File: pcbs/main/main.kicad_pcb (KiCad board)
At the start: 2 copper layers, 114 x 123.3 mm, 67 parts, among them J1 JST_XH_B3B, J2 JST_XH_B3B, J3 XT30PW-M, Q1 2SC945, Q2 2SC945, Q3 2SC945, Q4 2SC945, Q5 2SC945, Q6 2SC945, Q7 2SC945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

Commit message: Start layout
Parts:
- moved as3 189.5 mm to (79.1, 43.5)
- moved as4 189.5 mm to (79.1, 50.8)
- moved as1 162.9 mm to (101.0, 66.7), turned to 180 degrees
- moved C13 145.5 mm to (83.8, 124.7), turned to -90 degrees
- moved JP2 133.6 mm to (102.7, 71.6)
- moved JP1 132.6 mm to (99.2, 71.6)
- moved C5 129.1 mm to (97.0, 113.0), turned to -90 degrees
- moved C6 125.1 mm to (100.0, 113.0), turned to -90 degrees
- moved C7 121.3 mm to (103.0, 113.0), turned to -90 degrees
- moved C10 120.7 mm to (108.3, 51.8), turned to -173 degrees
- moved C12 119.8 mm to (108.3, 138.1), turned to 83 degrees
- moved C8 117.5 mm to (106.0, 113.0), turned to -90 degrees
- moved C2 106.9 mm to (139.2, 138.4), turned to 27.2 degrees
- moved C9 105.4 mm to (115.3, 138.1), turned to 83 degrees
- moved C3 103.7 mm to (113.9, 52.2), turned to 7 degrees
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
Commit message: Fix jumpers
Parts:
- removed JP1, JP2, JP3, JP4, JP5, JP6, JP7, JP8: Jumper_2_Open, Connector_PinHeader_2.54mm:PinHeader_1x02_P2.54mm_Vertical
- added J2: Jumpers, Connector_PinHeader_2.54mm:PinHeader_2x08_P2.54mm_Vertical, F.Cu at (106.1, 69.8)
- moved as2 151.5 mm to (100.4, 64.0), turned to 90 degrees
- moved as3 25.5 mm to (94.2, 64.0), turned to 90 degrees
- moved as4 15.8 mm to (87.8, 64.0), turned to 90 degrees
- moved as1 6.28 mm to (106.7, 64.0), turned to 90 degrees
- renumbered J2 to J3, J3 to J4
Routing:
- net /esp32/I2C.SDA: track 5.82 -> 34.5 mm
- net /esp32/I2C.SCL: track 6.50 -> 34.3 mm
- net Net-(J2-Pin_1): track 0.00 -> 8.69 mm
- net Net-(J2-Pin_9): track 0.00 -> 8.25 mm
- net Net-(J2-Pin_5): track 0.00 -> 8.21 mm
- net Net-(J2-Pin_13): track 0.00 -> 8.08 mm
- net Net-(J2-Pin_3): track 0.00 -> 6.01 mm
- net Net-(J2-Pin_7): track 0.00 -> 5.53 mm
- net Net-(J2-Pin_11): track 0.00 -> 5.04 mm
- net Net-(J2-Pin_15): track 0.00 -> 4.52 mm

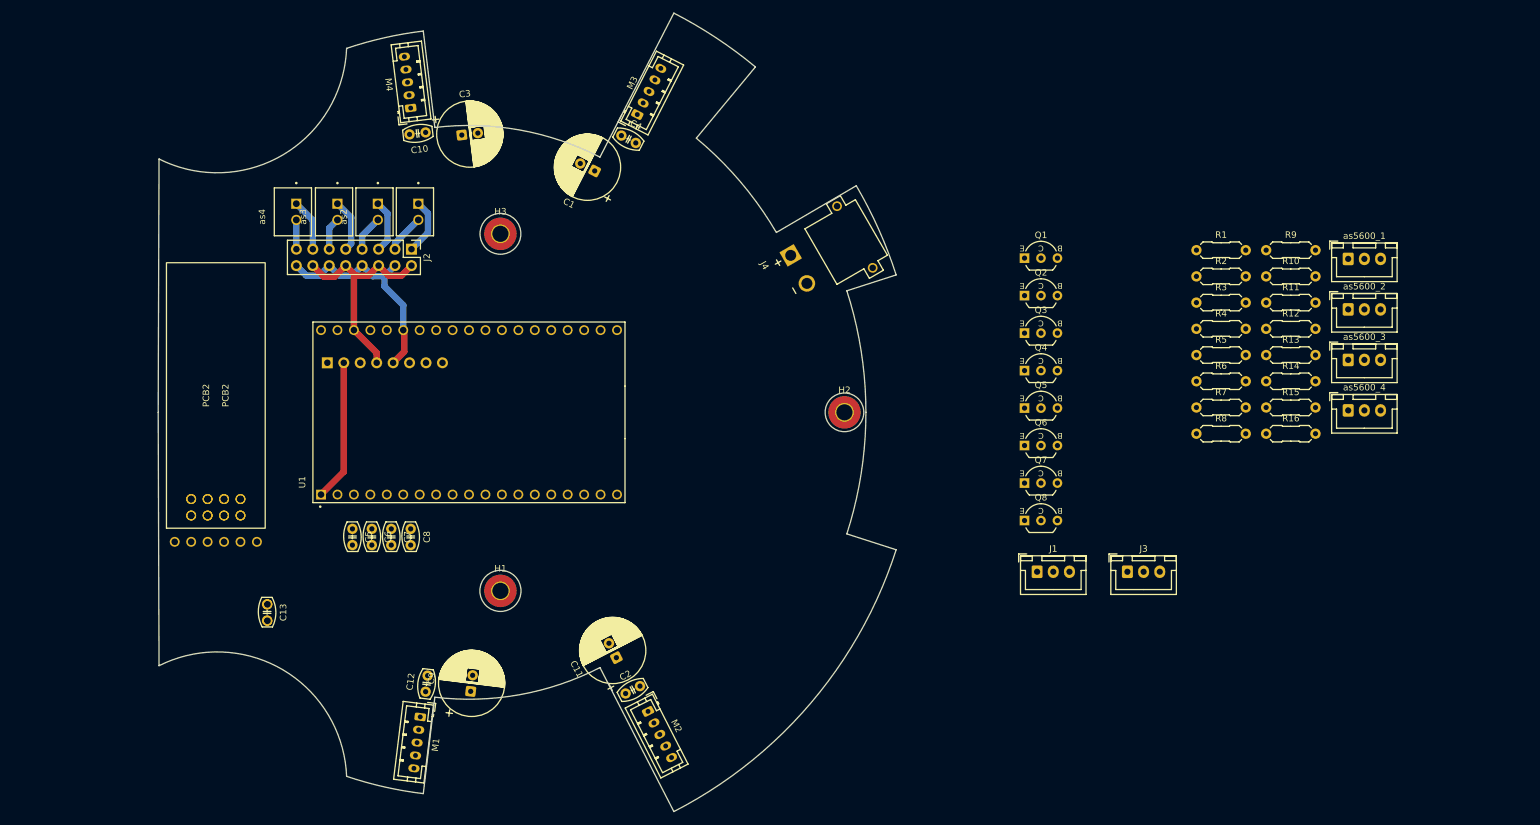
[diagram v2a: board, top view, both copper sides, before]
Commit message: Preliminary placing components
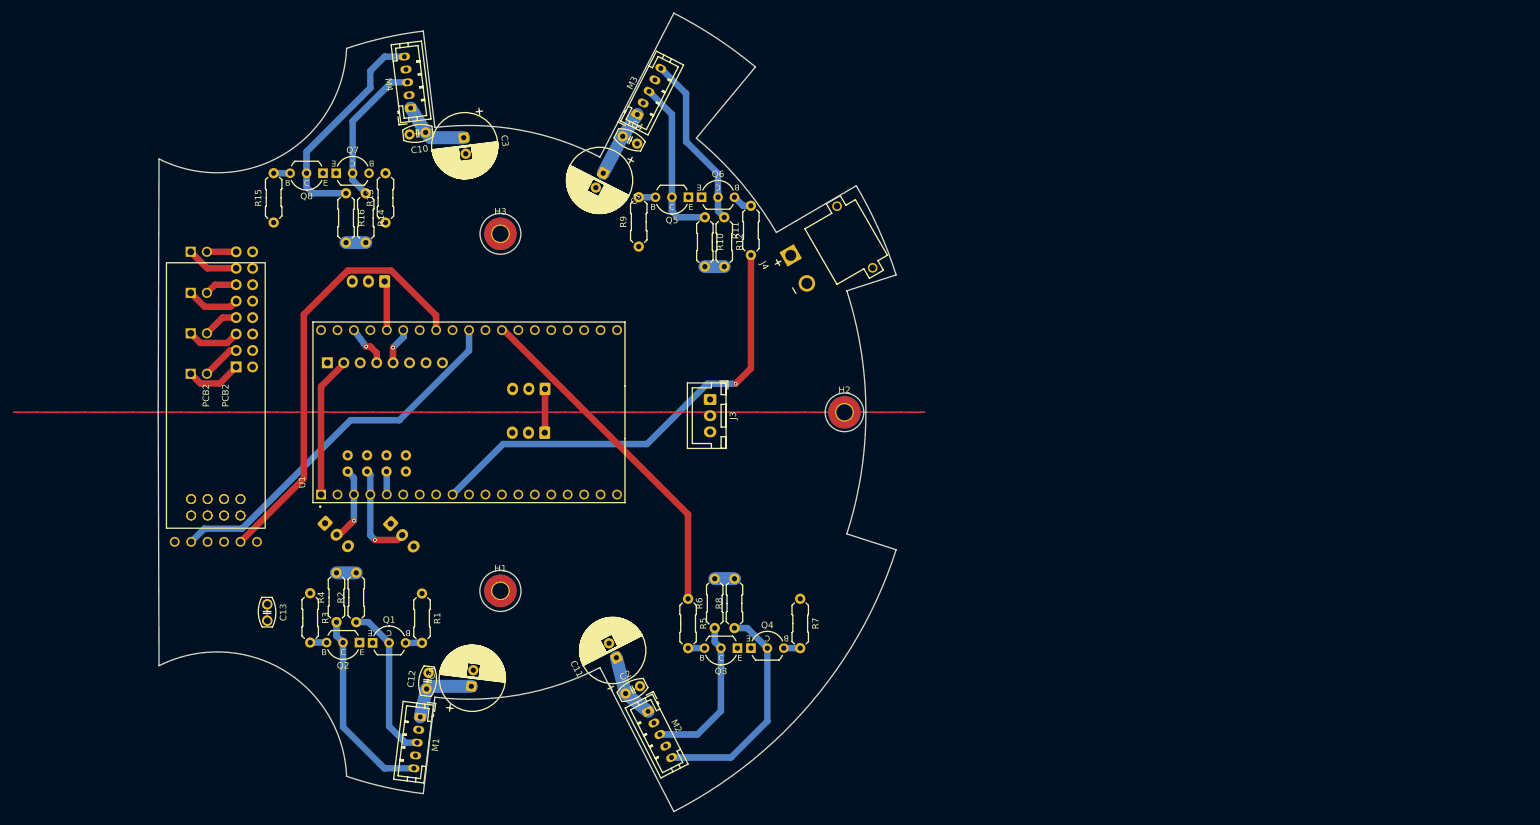
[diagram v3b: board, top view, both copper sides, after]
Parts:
- C5, C6, C7, C8, J1, J2, as1, as2, as3, as4, as5600_1, as5600_2, as5600_3, as5600_4: moved to B.Cu
- moved as5600_1 163.2 mm to (92.8, 112.1), turned to -45 degrees
- moved R15 155.9 mm to (84.8, 65.7), turned to 90 degrees
- moved as5600_2 151.5 mm to (102.9, 112.2), turned to -45 degrees
- moved R16 146.9 mm to (96.0, 61.2), turned to -90 degrees
- moved R3 144.1 mm to (90.5, 122.9), turned to -90 degrees
- moved R14 142.1 mm to (99.1, 61.2), turned to -90 degrees
- moved R4 140.3 mm to (94.5, 127.4), turned to 90 degrees
- moved R2 140.3 mm to (97.6, 127.4), turned to 90 degrees
- moved R13 137.6 mm to (102.1, 65.7), turned to 90 degrees
- moved R1 130.8 mm to (107.7, 123.0), turned to -90 degrees
- moved as5600_4 124.2 mm to (126.7, 98.1), turned to 180 degrees
- moved as5600_3 124.1 mm to (126.7, 91.4), turned to 180 degrees
- moved Q8 120.9 mm to (92.5, 58.1), turned to 180 degrees
- moved Q1 116.9 mm to (100.1, 130.6)
- moved Q7 116.6 mm to (94.5, 58.1)
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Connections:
- J3 pad 3: +3.3V -> +5V
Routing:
- net /esp32/M3_PWM: track 0.00 -> 71.7 mm, vias 0 -> 1
- net /esp32/RADIO.MISO: track 0.00 -> 67.5 mm
- net /esp32/RADIO.CS: track 0.00 -> 58.3 mm
- net /esp32/M2_DIR: track 0.00 -> 53.6 mm
- net +24V: track 0.00 -> 46.7 mm
- net Net-(M2-PWM): track 0.00 -> 34.8 mm
- net Net-(M4-PWM): track 0.00 -> 34.7 mm
- net Net-(M1-PWM): track 0.00 -> 30.2 mm
- net /esp32/I2C.SDA: track 34.5 -> 5.74 mm, vias 0 -> 1
- net Net-(M3-PWM): track 0.00 -> 27.8 mm
- net Net-(M3-DIR): track 0.00 -> 27.6 mm
- net /esp32/I2C.SCL: track 34.3 -> 6.73 mm, vias 0 -> 1
- net Net-(M1-DIR): track 0.00 -> 24.7 mm
- net Net-(M2-DIR): track 0.00 -> 24.2 mm
- net Net-(M4-DIR): track 0.00 -> 22.9 mm
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- added copper zone on B.Cu, net GND
- added copper zone on F.Cu, net GND

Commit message: Add step file
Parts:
- turned C12 to 173 degrees
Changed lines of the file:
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@@
 	(footprint "PCM_Capacitor_THT_AKL:C_Disc_D5.0mm_W2.5mm_P2.50mm"
 		(layer "F.Cu")
-		(at 108.458 137.7188 83)
+		(at 108.458 137.7188 173)
 		(descr "C, Disc series, Radial, pin pitch=2.50mm, , diameter*width=5*2.5mm^2, Capacitor, http://cdn-reichelt.de/documents/datenblatt/B300/DS_KERKO_TC.pdf, Alternate KiCad Library")
 		(tags "C Disc series Radial pin pitch 2.50mm  diameter 5mm width 2.5mm Capacitor")
 		(property "Reference" "C12"
-			(at 1.25 -2.5 83)
+			(at 1.25 -2.5 173)
 			(layer "F.SilkS")
 			(effects
@@
 		)
 		(property "Value" "100 nF"
-			(at 1.25 2.5 83)
+			(at 1.25 2.5 173)
 			(layer "F.Fab")
 			(hide yes)
@@
 		)
 		(property "Datasheet" "~"
-			(at 0 0 83)
+			(at 0 0 173)
 			(layer "F.Fab")
 			(hide yes)
@@
 		)
 		(property "Description" "Unpolarized capacitor"
-			(at 0 0 83)
+			(at 0 0 173)
 			(layer "F.Fab")
 			(hide yes)
@@
 		)
 		(fp_line
+			(start 1.524 0)
+			(end 1.397 0)
+			(stroke
+				(width 0.12)
+				(type solid)
+			)
+			(layer "F.SilkS")
+		)
+		(fp_line
+			(start 1.397 0)
+			(end 1.397 -0.6)
+			(stroke
+				(width 0.12)
+				(type solid)
+			)
+			(layer "F.SilkS")
+		)
+		(fp_line
+			(start 1.397 0)
+			(end 1.397 0.6)
+			(stroke
+				(width 0.12)
+				(type solid)
+			)
+			(layer "F.SilkS")
+		)
+		(fp_line
+			(start 1.1 0)
+			(end 1.1 -0.6)
+			(stroke
+				(width 0.12)
+				(type solid)
+			)
+			(layer "F.SilkS")
+		)
+		(fp_line
+			(start 1.1 0)
+			(end 1.1 0.6)
+			(stroke
+				(width 0.12)
+				(type solid)
+			)
+			(layer "F.SilkS")
+		)
+		(fp_line
 			(start 0.973 0)
 			(end 1.1 0)
@@
 		)
 		(fp_line
-			(start 1.1 0)
-			(end 1.1 -0.6)
-			(stroke
-				(width 0.12)
-				(type solid)
-			)
-			(layer "F.SilkS")
-		)
-		(fp_line
-			(start 1.1 0)
-			(end 1.1 0.6)
-			(stroke
-				(width 0.12)
-				(type solid)
-			)
-			(layer "F.SilkS")
-		)
-		(fp_line
-			(start 1.397 0)
-			(end 1.397 -0.6)
-			(stroke
-				(width 0.12)
-				(type solid)
-			)
-			(layer "F.SilkS")
-		)
-		(fp_line
-			(start 1.397 0)
-			(end 1.397 0.6)
-			(stroke
-				(width 0.12)
-				(type solid)
-			)
-			(layer "F.SilkS")
-		)
-		(fp_line
-			(start 1.524 0)
-			(end 1.397 0)
-			(stroke
-				(width 0.12)
-				(type solid)
-			)
-			(layer "F.SilkS")
-		)
-		(fp_line
 			(start -1.0795 0.8255)
 			(end -1.0795 -0.762)
+			(stroke
+				(width 0.12)
+				(type solid)
+			)
+			(layer "F.SilkS")
+		)
+		(fp_arc
+			(start 3.491127 0.759477)
+			(mid 1.21396 1.356434)
+			(end -1.0795 0.8255)
 			(stroke
 				(width 0.12)
@@
 			(layer "F.SilkS")
 		)
-		(fp_arc
-			(start 3.491127 0.759477)
-			(mid 1.21396 1.356434)
-			(end -1.0795 0.8255)
-			(stroke
-				(width 0.12)
-				(type solid)
-			)
-			(layer "F.SilkS")
+		(fp_line
+			(start 4 -1.5)
+			(end -1.5 -1.5)
+			(stroke
+				(width 0.05)
+				(type solid)
+			)
+			(layer "F.CrtYd")
+		)
+		(fp_line
+			(start 4 1.5)
+			(end 4 -1.5)
+			(stroke
+				(width 0.05)
+				(type solid)
+			)
+			(layer "F.CrtYd")
 		)
 		(fp_line
@@
 		)
 		(fp_line
-			(start 4 -1.5)
-			(end -1.5 -1.5)
-			(stroke
-				(width 0.05)
-				(type solid)
-			)
-			(layer "F.CrtYd")
-		)
-		(fp_line
 			(start -1.5 1.5)
 			(end 4 1.5)
@@
 		)
 		(fp_line
-			(start 4 1.5)
-			(end 4 -1.5)
-			(stroke
-				(width 0.05)
-				(type solid)
-			)
-			(layer "F.CrtYd")
+			(start 3.75 -1.25)
+			(end -1.25 -1.25)
+			(stroke
+				(width 0.1)
+				(type solid)
+			)
+			(layer "F.Fab")
+		)
+		(fp_line
+			(start 3.75 1.25)
+			(end 3.75 -1.25)
+			(stroke
+				(width 0.1)
+				(type solid)
+			)
+			(layer "F.Fab")
 		)
 		(fp_line
@@
 		)
 		(fp_line
-			(start 3.75 -1.25)
-			(end -1.25 -1.25)
-			(stroke
-				(width 0.1)
-				(type solid)
-			)
-			(layer "F.Fab")
-		)
-		(fp_line
 			(start -1.25 1.25)
 			(end 3.75 1.25)
@@
 			(layer "F.Fab")
 		)
-		(fp_line
-			(start 3.75 1.25)
-			(end 3.75 -1.25)
-			(stroke
-				(width 0.1)
-				(type solid)
-			)
-			(layer "F.Fab")
-		)
 		(fp_text user "${REFERENCE}"
-			(at 1.25 0 83)
+			(at 1.25 0 173)
 			(layer "F.Fab")
 			(effects
@@
 		)
 		(pad "1" thru_hole circle
-			(at 0 0 83)
+			(at 0 0 173)
 			(size 1.6 1.6)
 			(drill 0.8)
@@
 		)
 		(pad "2" thru_hole circle
-			(at 2.5 0 83)
+			(at 2.5 0 173)
 			(size 1.6 1.6)
 			(drill 0.8)

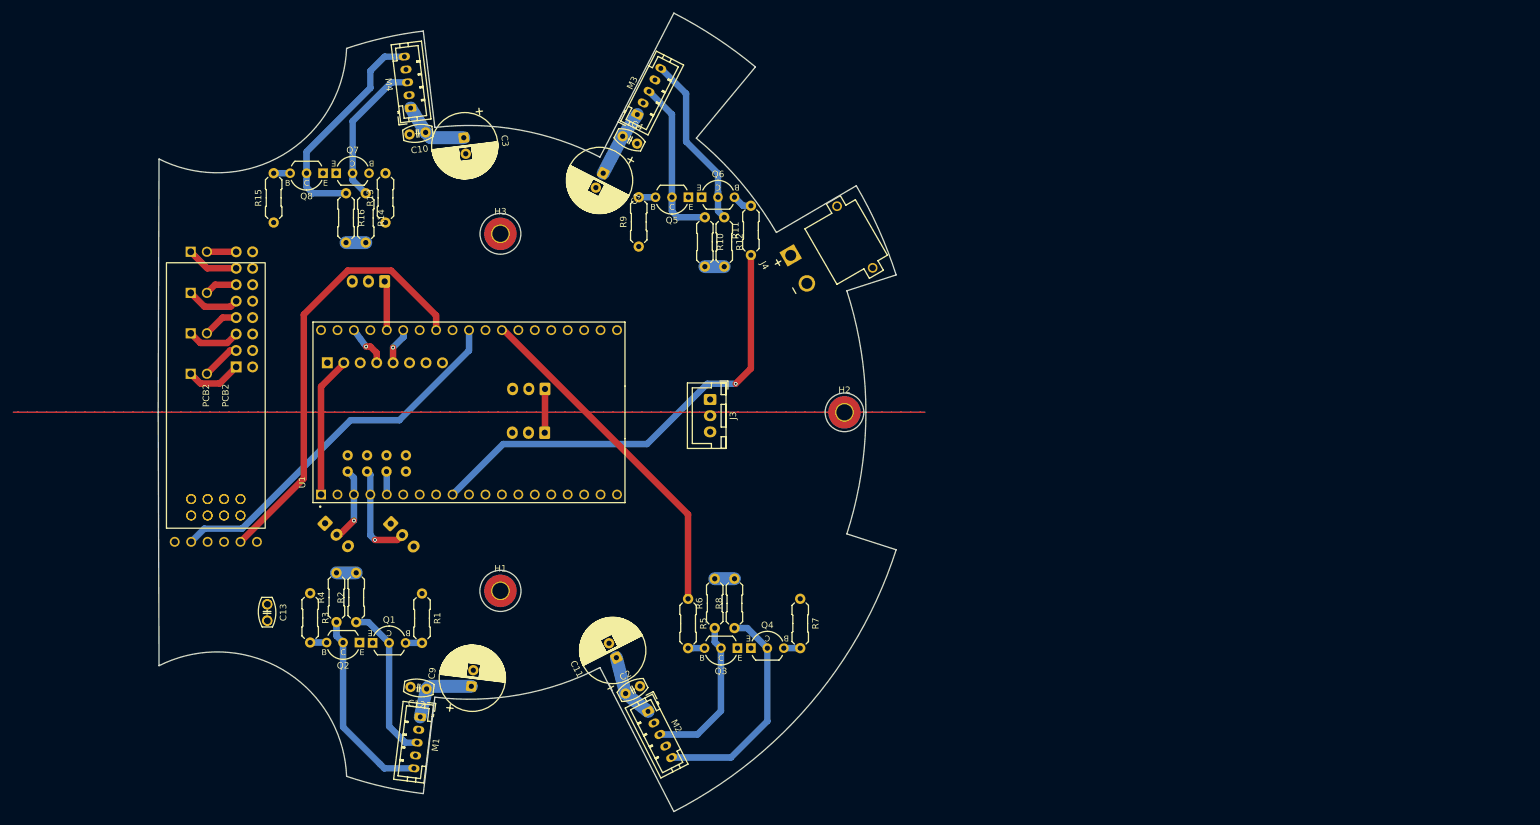
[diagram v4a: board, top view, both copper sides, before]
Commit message: feat: roteamento do main PCB
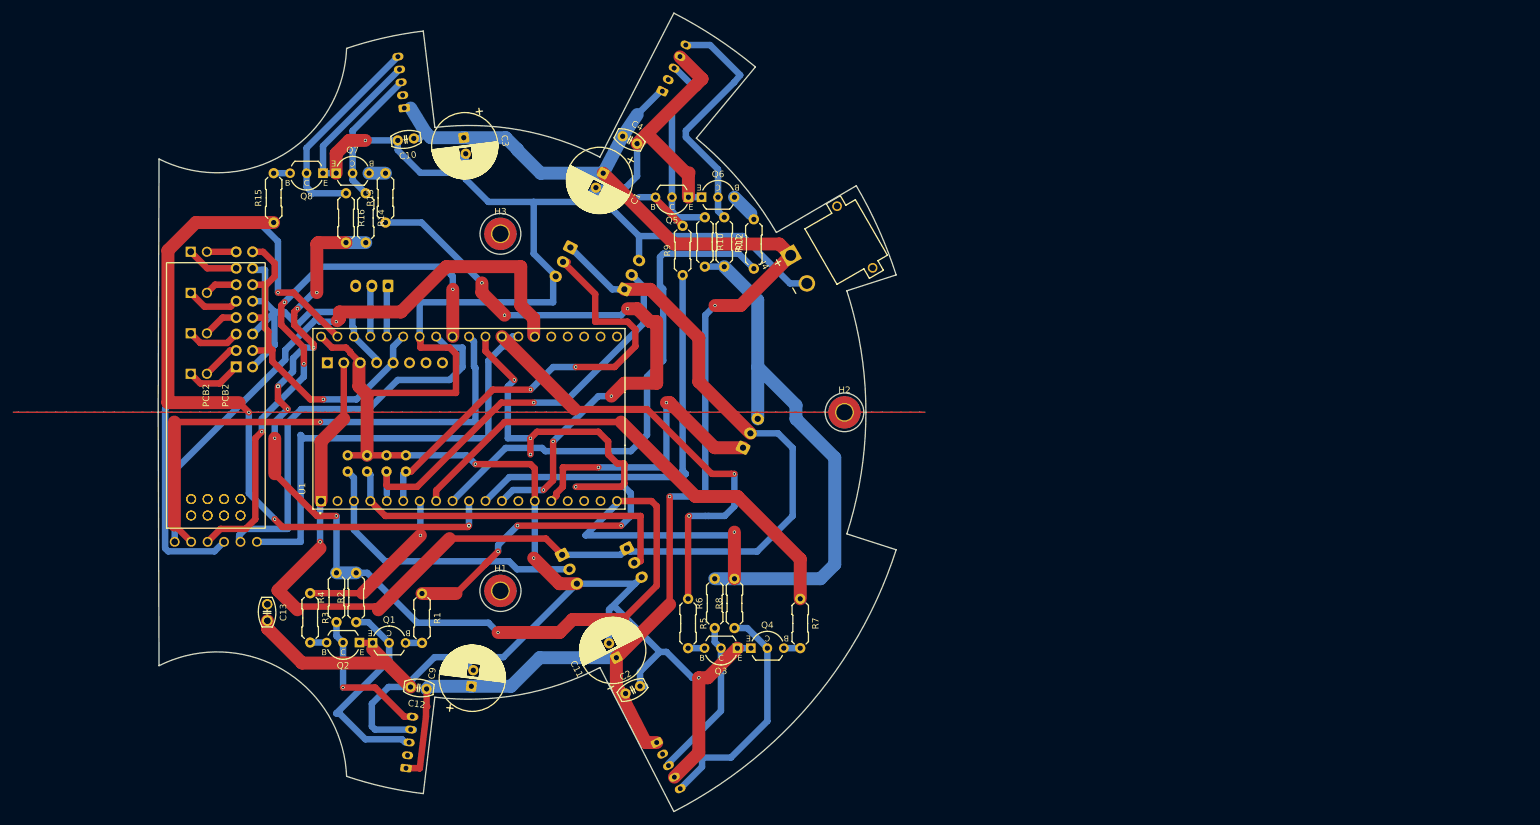
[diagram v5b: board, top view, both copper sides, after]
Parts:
- J3, M1, M2, M3, M4: moved to B.Cu
- moved as5600_1 36.9 mm to (129.4, 117.0), turned to -63 degrees
- moved as5600_2 36.7 mm to (139.4, 116.0), turned to -63 degrees
- moved as5600_4 28.9 mm to (130.7, 69.5), turned to -117 degrees
- moved as5600_3 19.7 mm to (139.0, 76.0), turned to 63 degrees
- moved J3 9.02 mm to (157.3, 100.5), turned to 63 degrees
- moved M1 8.21 mm to (105.3, 150.0), turned to 83 degrees
- moved R9 8.09 mm to (148.0, 73.8)
- moved M3 5.29 mm to (144.9, 45.4)
- moved M2 4.99 mm to (144.0, 146.0)
- moved R11 2.14 mm to (159.0, 72.8)
- moved C10 2.05 mm to (106.5, 52.7)
- moved M4 1.00 mm to (105.0, 48.0)
- moved U1 1.00 mm to (115.0, 96.0)
- moved J1 0.87 mm to (102.5, 75.5)
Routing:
- net GND: track 0.00 -> 474.5 mm, vias 0 -> 4
- net +5V: track 12.1 -> 268.0 mm, vias 0 -> 9
- net +24V: track 46.7 -> 228.4 mm, vias 0 -> 2
- net +3.3V: track 28.6 -> 190.6 mm, vias 0 -> 1
- net /esp32/M4_PWM: track 0.00 -> 107.3 mm, vias 0 -> 3
- net /esp32/M1_DIR: track 0.00 -> 104.5 mm, vias 0 -> 7
- net /esp32/RADIO.MOSI: track 0.00 -> 95.7 mm, vias 0 -> 1
- net /esp32/M4_DIR: track 0.00 -> 94.4 mm, vias 0 -> 6
- net /esp32/RADIO.CE: track 0.00 -> 90.7 mm, vias 0 -> 1
- net /esp32/RADIO.CLK: track 0.00 -> 85.3 mm, vias 0 -> 4
- net /esp32/M2_PWM: track 0.00 -> 77.1 mm
- net /esp32/RADIO.IRQ: track 0.00 -> 70.9 mm
- net /esp32/M4_ENC: track 0.00 -> 69.5 mm, vias 0 -> 2
- net /esp32/M3_DIR: track 0.00 -> 63.6 mm
- net /esp32/M3_ENC: track 3.61 -> 64.2 mm, vias 0 -> 1
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
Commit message: Re-routing
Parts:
- J3: moved to F.Cu
- moved as5600_2 57.4 mm to (88.6, 89.2), turned to 0 degrees
- moved C13 54.6 mm to (72.0, 71.3), turned to 90 degrees
- moved J3 46.4 mm to (113.2, 114.8), turned to 180 degrees
- moved as5600_1 43.9 mm to (88.6, 100.8), turned to 0 degrees
- moved PCB1 42.1 mm to (76.0, 76.9), turned to 90 degrees
- moved J2 32.9 mm to (78.7, 120.8)
- moved as1 32.9 mm to (72.9, 121.4)
- moved as2 32.9 mm to (72.9, 115.1)
- moved as3 32.9 mm to (72.9, 108.9)
- moved as4 32.9 mm to (72.9, 102.5)
- moved as5600_4 31.5 mm to (134.5, 100.8), turned to 0 degrees
- moved C7 16.6 mm to (118.8, 103.2)
- moved C8 16.6 mm to (121.8, 103.2), turned to 0 degrees
- moved U1 16.5 mm to (131.5, 95.0)
- moved C5 16.5 mm to (112.7, 103.2), turned to 180 degrees
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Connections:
- C13 pad 1: +3V3 -> +3.3V
- PCB1 pad 15: +3V3 -> +3.3V
- U1 pad 10: /esp32/M4_PWM -> /esp32/M2_PWM
- U1 pad 12: /esp32/M4_DIR -> /esp32/M3_PWM
- U1 pad 27: /esp32/M2_DIR -> /esp32/M4_PWM
- U1 pad 28: /esp32/M1_DIR -> /esp32/M4_DIR
- U1 pad 8: /esp32/M2_PWM -> /esp32/M1_DIR
- U1 pad 9: /esp32/M3_PWM -> /esp32/M2_DIR
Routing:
- net GND: track 474.5 -> 3.89 mm, vias 4 -> 0
- net /esp32/M1_DIR: track 104.5 -> 26.5 mm, vias 7 -> 0
- net /esp32/RADIO.MOSI: track 95.7 -> 42.9 mm
- net /esp32/M4_DIR: track 94.4 -> 45.5 mm, vias 6 -> 1
- net /esp32/M4_ENC: track 69.5 -> 23.6 mm, vias 2 -> 0
- net /esp32/M4_PWM: track 107.3 -> 67.0 mm, vias 3 -> 1
- net +3.3V: track 190.6 -> 154.6 mm, vias 1 -> 2
- net /esp32/M2_DIR: track 70.2 -> 35.5 mm, vias 2 -> 0
- net /esp32/M3_ENC: track 64.2 -> 29.6 mm, vias 1 -> 0
- net /esp32/I2C.SDA: track 55.6 -> 88.3 mm, vias 1 -> 3
- net /esp32/M2_PWM: track 77.1 -> 48.1 mm, vias 0 -> 1
- net /esp32/RADIO.CE: track 90.7 -> 62.0 mm
- net /esp32/RADIO.CLK: track 85.3 -> 57.3 mm, vias 4 -> 1
- net /esp32/M3_PWM: track 79.1 -> 51.9 mm
- net /esp32/I2C.SCL: track 49.4 -> 75.8 mm, vias 0 -> 6
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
